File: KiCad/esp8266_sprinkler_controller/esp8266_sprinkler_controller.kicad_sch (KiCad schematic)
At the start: 22 parts, among them J1 Barrel_Jack_Switch, J2 Screw_Terminal_01x02 ST1, J3 Screw_Terminal_01x02 ST2, J4 Screw_Terminal_01x02 ST3, J5 Screw_Terminal_01x02 ST4, SW1 SW_Push, U1 LM7805_TO220, U2 WeMos_D1_mini, U3 74HC595, U4 L293D, U5 L293D

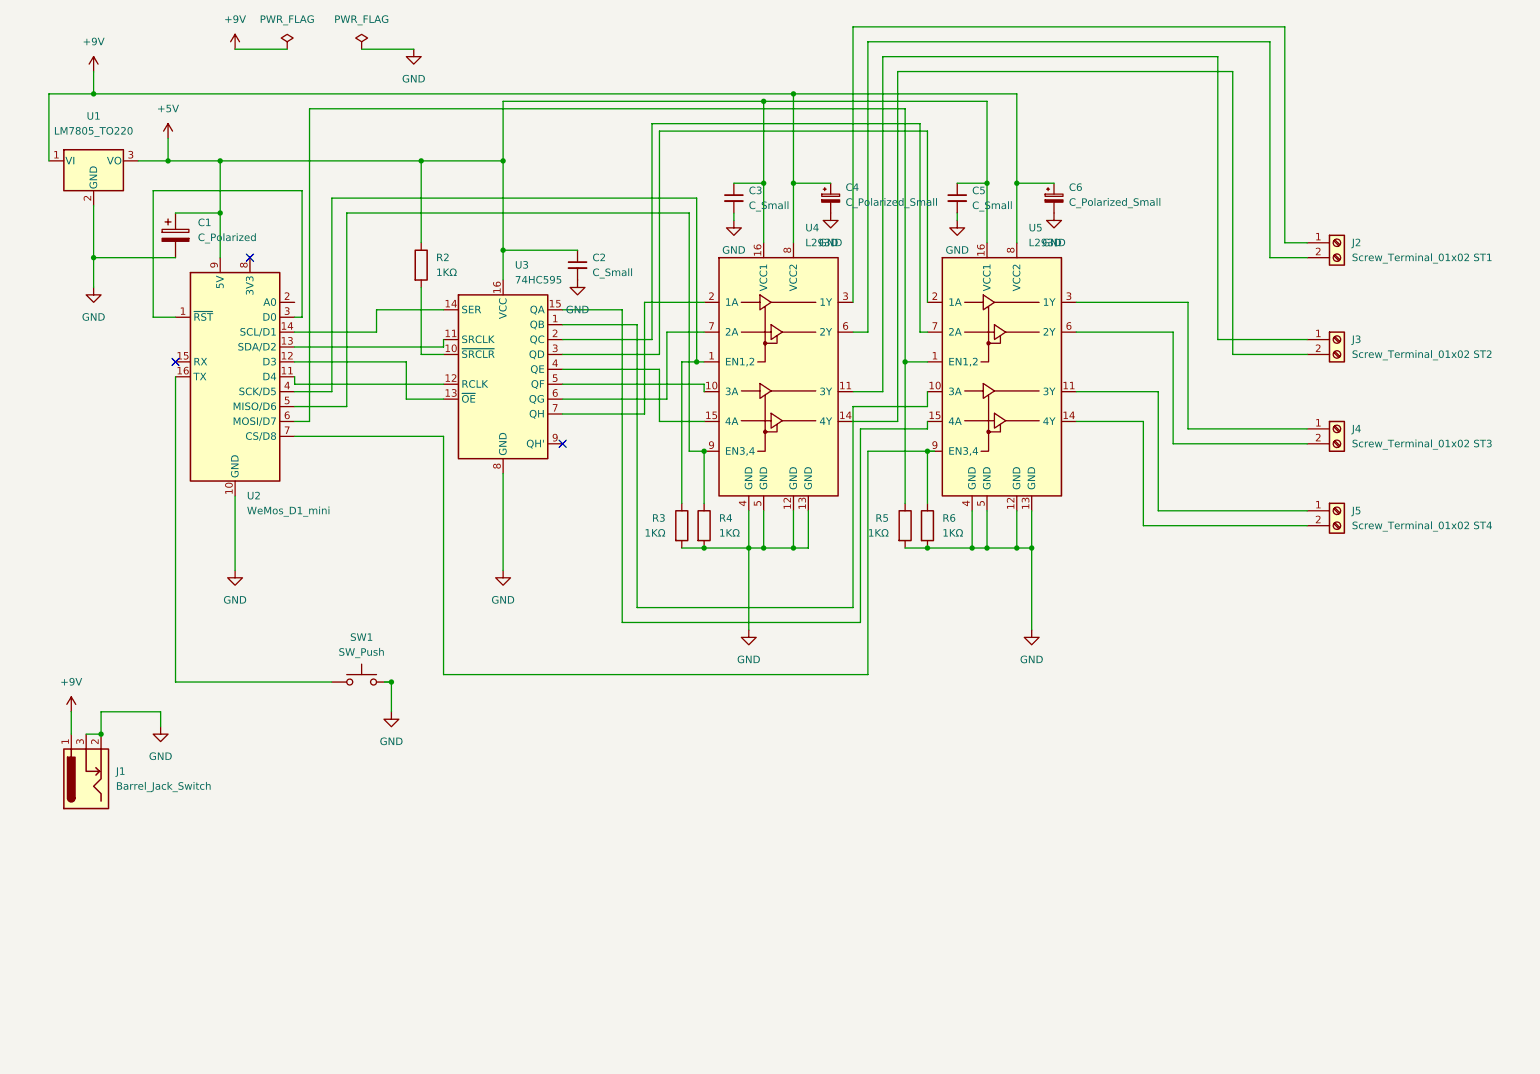
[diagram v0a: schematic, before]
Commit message: Researching a way to use less power when the circuit is in deep sleep; Updated Kicad schematic and pcb design
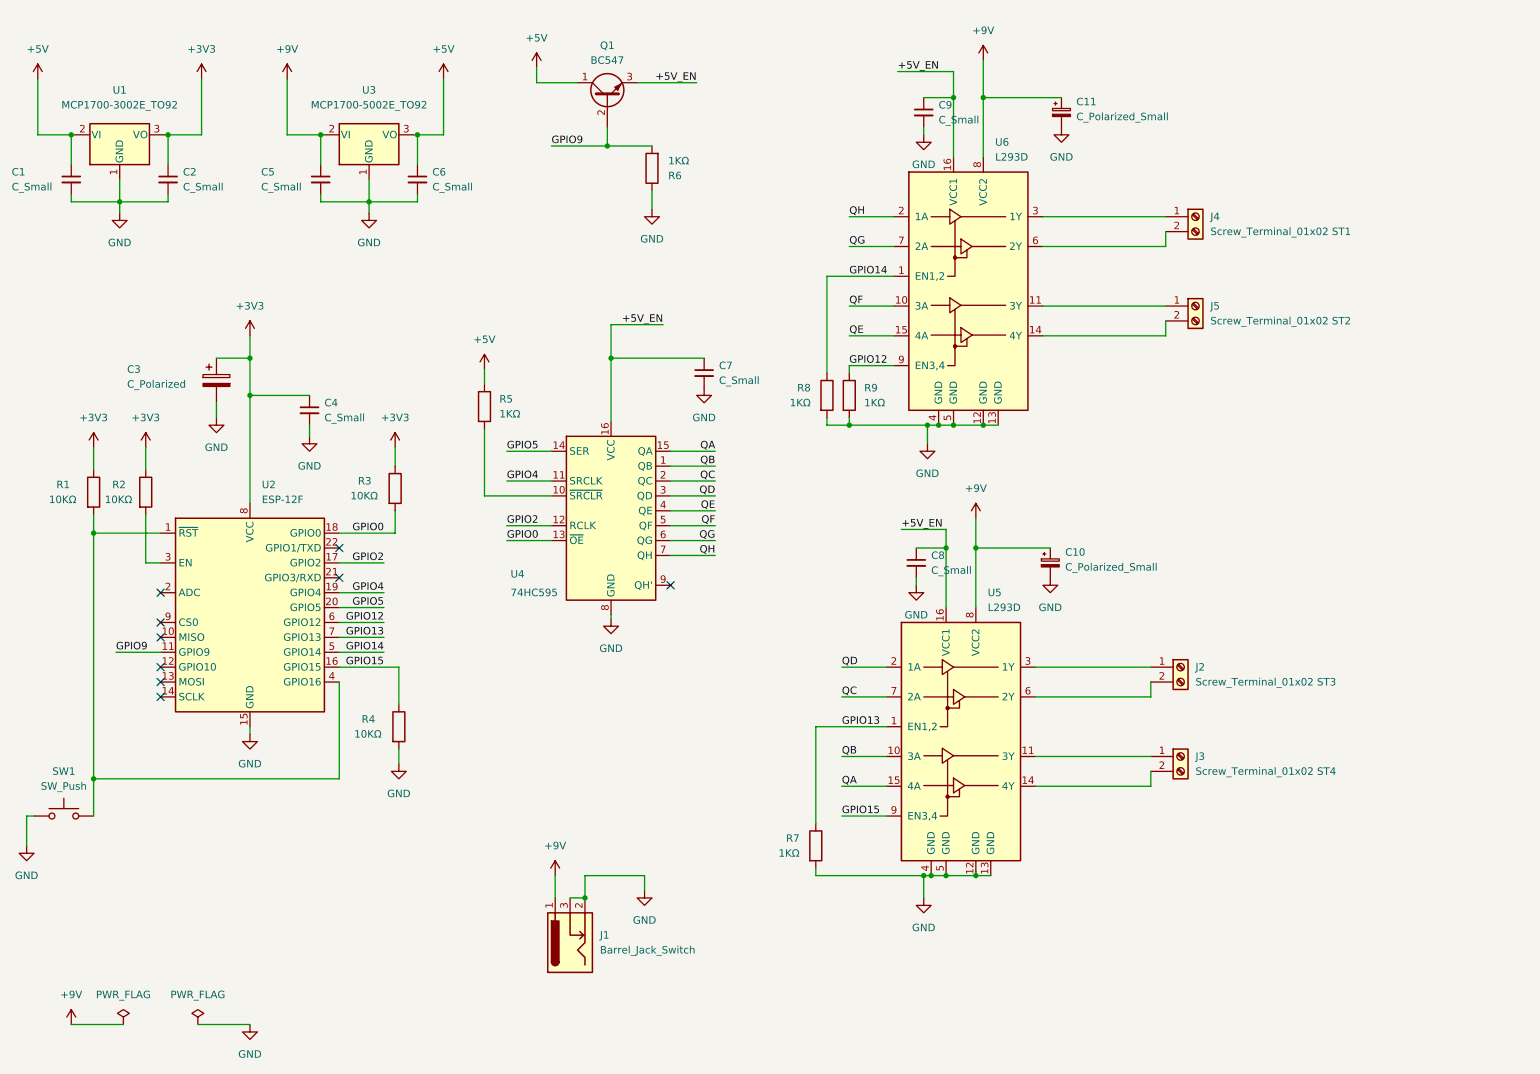
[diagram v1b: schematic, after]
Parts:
- removed C1: C_Polarized, Capacitor_THT:CP_Radial_D4.0mm_P2.00mm, symbol Device:C_Polarized
- removed R5: 1KΩ, Resistor_THT:R_Axial_DIN0207_L6.3mm_D2.5mm_P7.62mm_Horizontal, symbol Device:R
- removed U1: LM7805_TO220, Package_TO_SOT_THT:TO-220-3_Horizontal_TabDown, symbol Regulator_Linear:LM7805_TO220
- removed U2: WeMos_D1_mini, Module:WEMOS_D1_mini_light, symbol MCU_Module:WeMos_D1_mini
- added C1, C2, C4, C5, C6: C_Small, Capacitor_THT:C_Disc_D3.0mm_W1.6mm_P2.50mm, symbol Device:C_Small
- added C3: C_Polarized, Capacitor_THT:CP_Radial_D4.0mm_P2.00mm, symbol Device:C_Polarized
- added Q1: BC547, Package_TO_SOT_THT:TO-92_Inline, symbol Transistor_BJT:BC547
- added R1, R2: 10KΩ, Resistor_THT:R_Axial_DIN0207_L6.3mm_D2.5mm_P7.62mm_Horizontal, symbol Device:R
- added R7, R8, R9: 1KΩ, Resistor_THT:R_Axial_DIN0207_L6.3mm_D2.5mm_P7.62mm_Horizontal, symbol Device:R
- added U1: MCP1700-3002E_TO92, Package_TO_SOT_THT:TO-92_Inline, symbol Regulator_Linear:MCP1700-3002E_TO92
- added U2: ESP-12F, RF_Module:ESP-12E, symbol RF_Module:ESP-12F
- added U3: MCP1700-5002E_TO92, Package_TO_SOT_THT:TO-92, symbol Regulator_Linear:MCP1700-5002E_TO92
- R3, R4: value 1KΩ -> 10KΩ
- U4: renamed from U3; footprint Package_DIP:DIP-16_W7.62mm -> Package_DIP:DIP-16_W7.62mm_Socket
- U5: footprint Package_DIP:DIP-16_W7.62mm -> Package_DIP:DIP-16_W7.62mm_Socket
- U6: renamed from U4; footprint Package_DIP:DIP-16_W7.62mm -> Package_DIP:DIP-16_W7.62mm_Socket
- renumbered C6 to C10, C4 to C11, C2 to C7, C5 to C8, C3 to C9, J4 to J2, J5 to J3, J2 to J4, J3 to J5, R2 to R5
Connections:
- net +5V: now also C1.1, C6.1, Q1.1 (C), U1.2 (VI), U3.3 (VO); no longer C7.1, C8.1, C9.1, U4.16 (VCC), U5.16 (VCC1), U6.16 (VCC1)
- net +9V: now also C5.1, U3.2 (VI)
- net GND: now also R6.1, SW1.1, C1.2, C2.2, C3.2, C4.2, C5.2, C6.2, R7.2, R8.2, R9.2, U1.1 (GND), U2.15 (GND), U3.1 (GND); no longer R3.2, R6.2, SW1.2
- net GPIO15: now reaches U5.9 (EN3,4)
- net GPIO15: now also R4.1, U2.16 (GPIO15); no longer R6.1
- net +3V3: now reaches R3.1
- net +3V3: now also C2.1, C3.1, C4.1, R1.1, R2.1, U1.3 (VO), U2.8 (VCC); no longer U6.1 (EN1,2)
- net QF: now reaches U4.5 (QF), U6.10 (3A)
- net QE: now reaches U4.4 (QE), U6.15 (4A)
- net QH: now reaches U4.7 (QH), U6.2 (1A)
- net QG: now reaches U4.6 (QG), U6.7 (2A)
- net GPIO12: now reaches U6.9 (EN3,4)
- net GPIO12: now also R9.1, U2.6 (GPIO12); no longer R4.1
- net GPIO2: now reaches U4.12 (RCLK)
- net GPIO2: now also U2.17 (GPIO2)
- net GPIO0: now reaches U4.13 (~{OE})
- net GPIO0: now also R3.2, U2.18 (GPIO0)
- net GPIO4: now reaches U4.11 (SRCLK)
- net GPIO4: now also U2.19 (GPIO4)
- net GPIO5: now reaches U4.14 (SER)
- net GPIO5: now also U2.20 (GPIO5)
- net GPIO13: now reaches U5.1 (EN1,2)
- net GPIO13: now also R7.1, U2.7 (GPIO13)
- net QB: now reaches U4.1 (QB), U5.10 (3A)
- net QA: now reaches U4.15 (QA), U5.15 (4A)
- net QC: now reaches U4.2 (QC), U5.7 (2A)
- net QD: now reaches U4.3 (QD), U5.2 (1A)
- new net: R2.2, U2.3 (EN)
- new net: R1.2, SW1.2, U2.1 (~{RST}), U2.4 (GPIO16)
- new net +5V_EN: C7.1, C8.1, C9.1, Q1.3 (E), U4.16 (VCC), U5.16 (VCC1), U6.16 (VCC1)
- new net GPIO14: R8.1, U2.5 (GPIO14), U6.1 (EN1,2)
- new net GPIO9: Q1.2 (B), R6.2, U2.11 (GPIO9)
- no-connect marks 3 -> 9
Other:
- moved on the sheet: C10, C11, C7, C8, C9, J1, J2, J3, J4, J5, R5, SW1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

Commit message: Refactor esp8266 code; New Kicad schematic version (v2.0) to make the circuit battery efficient
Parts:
- added D1: D_Schottky, Diode_THT:D_A-405_P7.62mm_Horizontal, symbol Device:D_Schottky
- R6: value 1KΩ -> 10KΩ
- renumbered C5 to C1, C6 to C2, C1 to C5, C2 to C6, U3 to U1, U1 to U3
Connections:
- net +5V: now also C7.1, C8.1, C9.1, U4.16 (VCC), U5.16 (VCC1), U6.16 (VCC1); no longer Q1.1 (C)
- net GND: now also Q1.3 (E); no longer R6.1, R7.2, R8.2, R9.2, U4.8 (GND), U5.12 (GND), U5.13 (GND), U5.4 (GND), U5.5 (GND), U6.12 (GND), U6.13 (GND), U6.4 (GND), U6.5 (GND)
- net GPIO15: now also D1.2 (A); no longer U5.9 (EN3,4)
- net GPIO5: now also R6.1; no longer U4.14 (SER)
- net GPIO3: now reaches U2.21 (GPIO3/RXD)
- net GPIO3: now also U4.14 (SER)
- removed net +5V_EN: C7.1, C8.1, C9.1, Q1.3 (E), U4.16 (VCC), U5.16 (VCC1), U6.16 (VCC1)
- net GPIO9: no longer names the net of Q1.2 (B), R6.2
- net GPIO9: no longer U2.11 (GPIO9)
- new net: D1.1 (K), U5.9 (EN3,4)
- new net GND_EN: Q1.1 (C), R7.2, R8.2, R9.2, U4.8 (GND), U5.12 (GND), U5.13 (GND), U5.4 (GND), U5.5 (GND), U6.12 (GND), U6.13 (GND), U6.4 (GND), U6.5 (GND)
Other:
- moved on the sheet: C1, C2, C5, C6, Q1, U1, U3

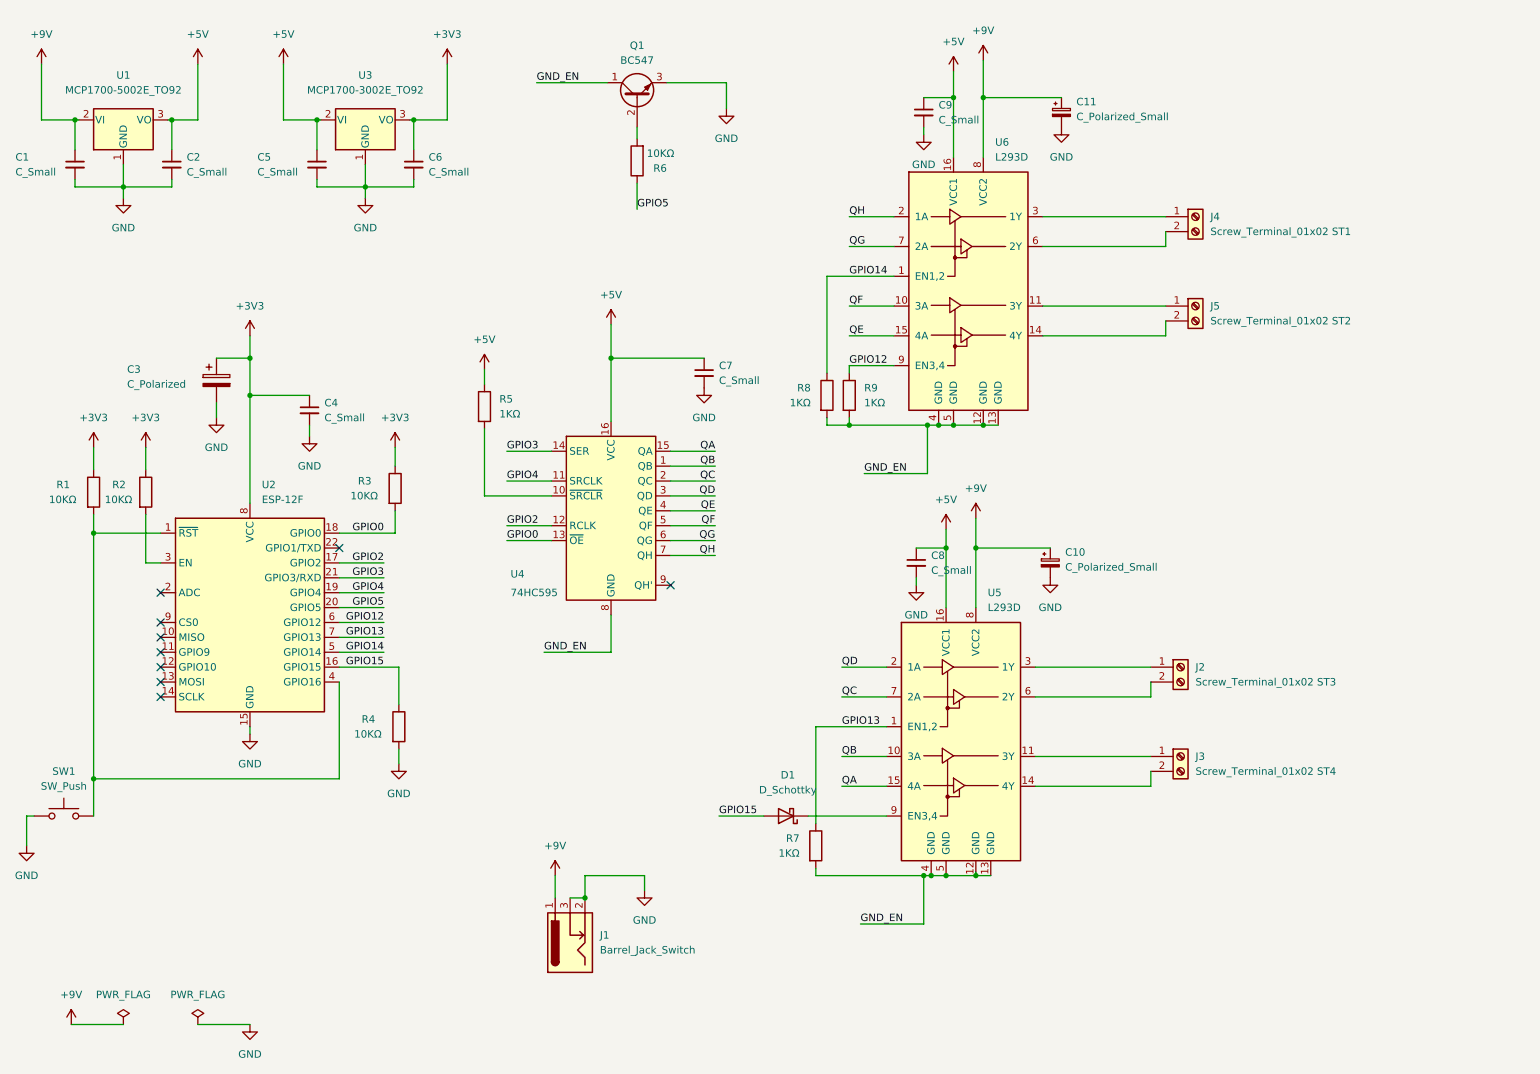
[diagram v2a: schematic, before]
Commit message: KiCad: Revision 3 of schematic abdnd PCB. Solved a couple of circuit problems:  - Added a Schottky Diode between the reset line and GPIO16    so this pin is not shorted when the reset button is pressed.  - Added a Schottky Diode between GPIO15 and the enable pin of the L293D
ESP8266: Force a loop call to the MQTT broker when interface_mode is not active
as MQTT messages were not being published correctly because the ESP8266 would
go into deep sleep before it finished processing the messages.
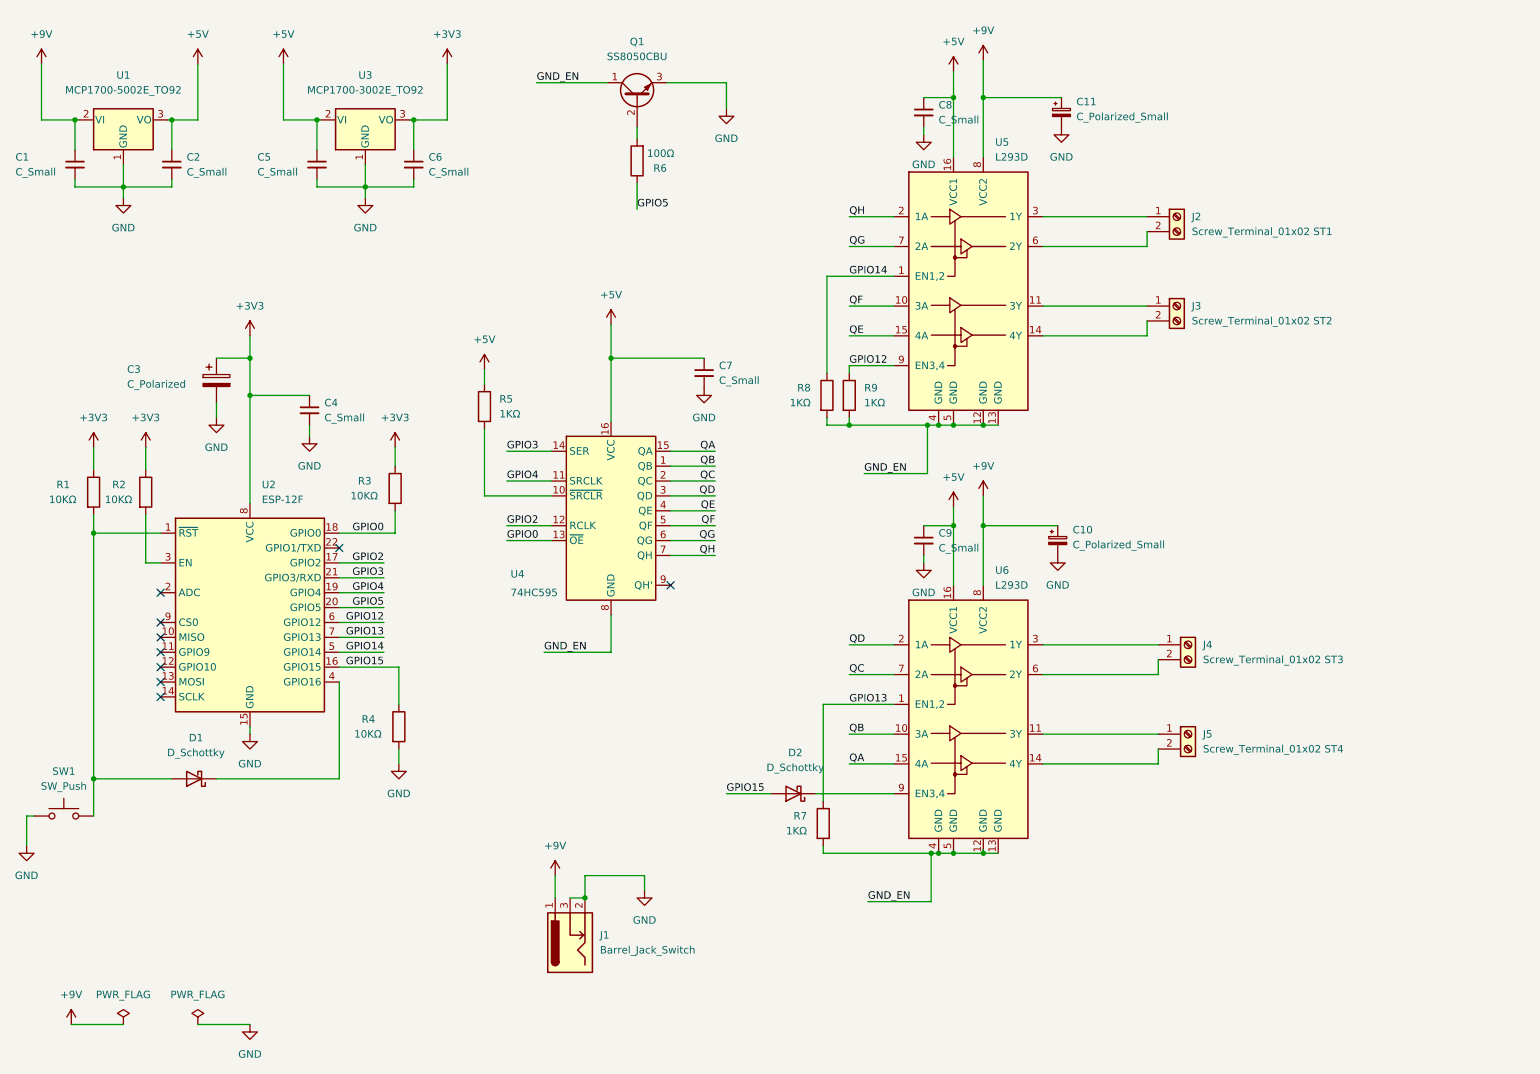
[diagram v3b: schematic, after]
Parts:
- added D1: D_Schottky, Diode_THT:D_A-405_P7.62mm_Horizontal, symbol Device:D_Schottky
- Q1: value BC547 -> SS8050CBU; footprint Package_TO_SOT_THT:TO-92_Inline -> Package_TO_SOT_THT:TO-92
- R6: value 10KΩ -> 100Ω
- U3: footprint Package_TO_SOT_THT:TO-92_Inline -> Package_TO_SOT_THT:TO-92
- renumbered C9 to C8, C8 to C9, D1 to D2, J4 to J2, J5 to J3, J2 to J4, J3 to J5, U6 to U5, U5 to U6
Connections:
- net at R1.2, SW1.2, U2.1 (~{RST}): now also D1.2 (A); no longer U2.4 (GPIO16)
- new net: D1.1 (K), U2.4 (GPIO16)
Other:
- moved on the sheet: C10, C9, D2, J2, J3, J4, J5, R7, U6
